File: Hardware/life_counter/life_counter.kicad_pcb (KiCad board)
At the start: 2 copper layers, 133.4 x 75.6 mm, 46 parts, among them J1 XIAO_BAT_LINK, P1 OLED-DISPLAY, Q1 Q-PMOS, U1 XIAO ESP32C3

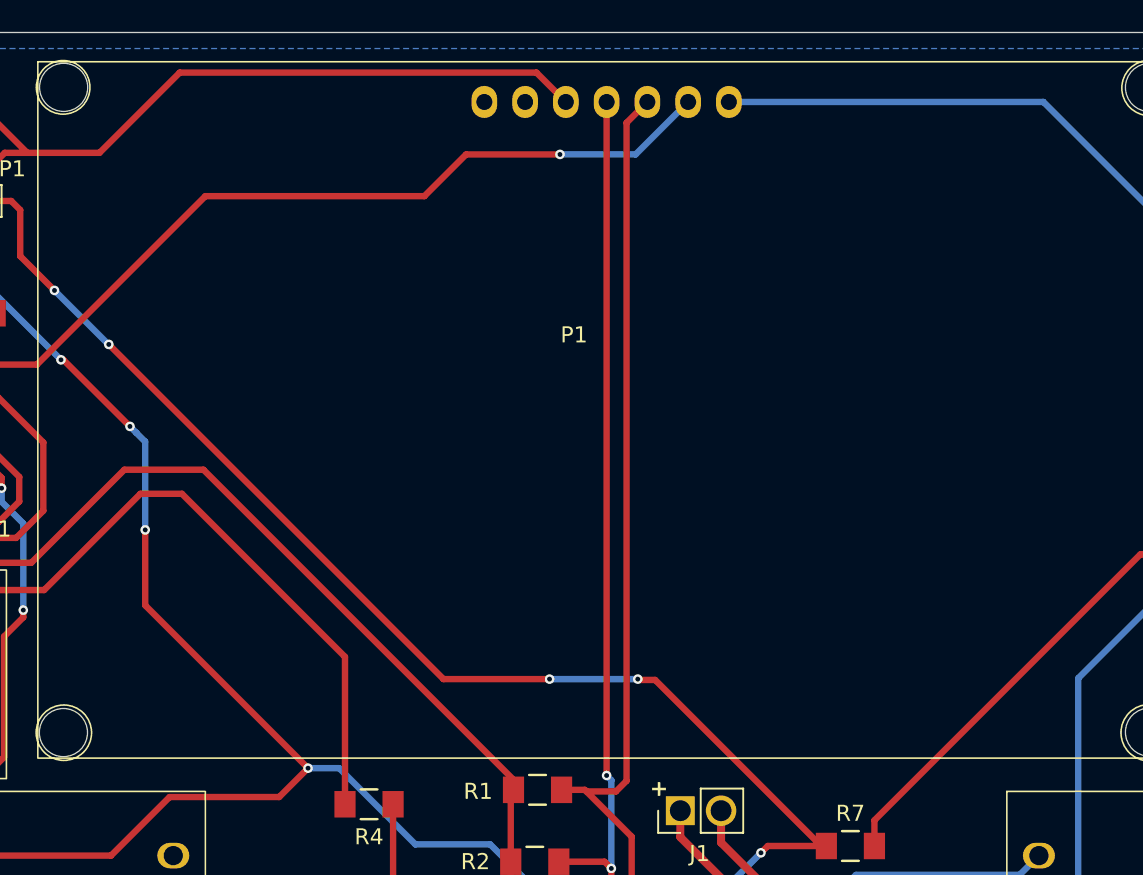
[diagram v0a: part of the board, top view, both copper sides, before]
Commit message: updated the kicad schematics, added auto shut off when battery is at 3.3V, added an image folder forthe  github page
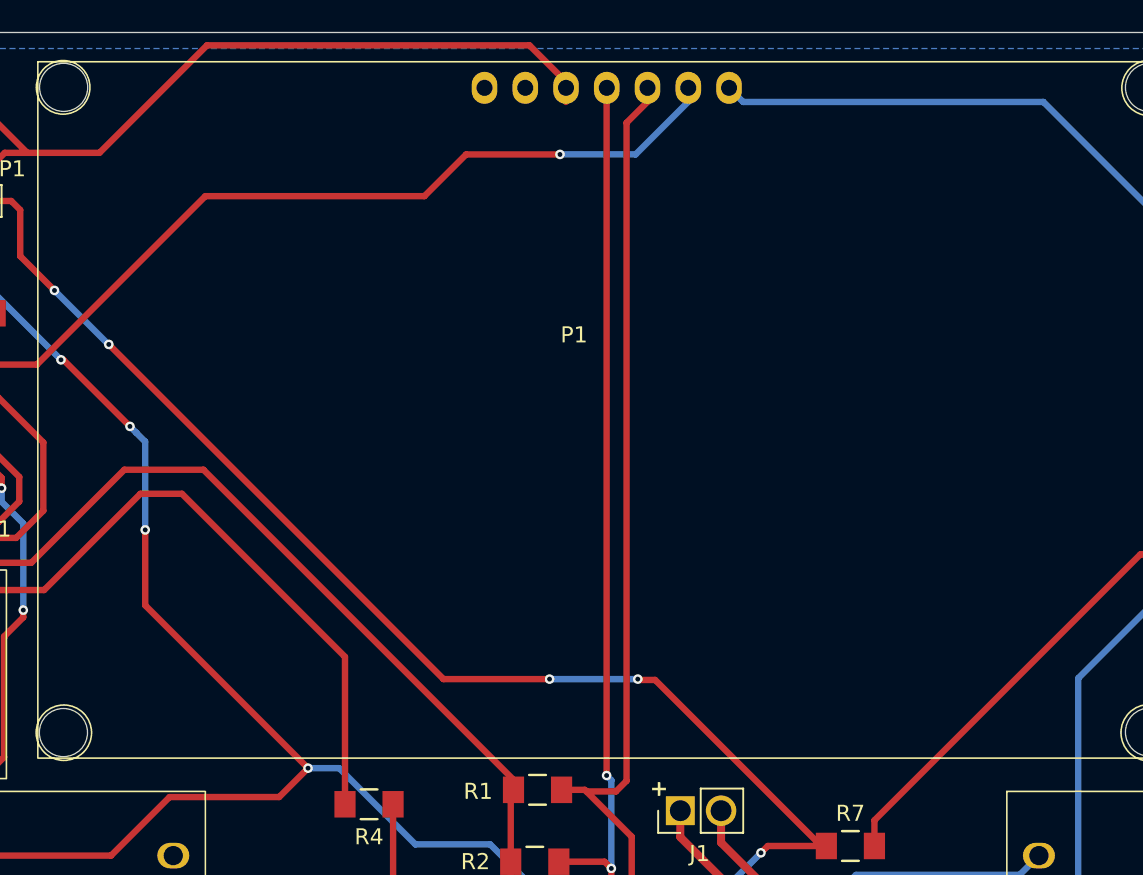
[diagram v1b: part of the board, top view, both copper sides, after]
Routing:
- net Net-(P1-RES): track 75.9 -> 78.0 mm
- net /SDA: track 64.3 -> 65.1 mm
- net /SCL: track 63.0 -> 63.9 mm
- net Net-(DISP_BYP1-B): track 87.8 -> 88.7 mm
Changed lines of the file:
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@@
 		)
 		(pad "1" thru_hole oval
-			(at 9.65 -15.02 270)
+			(at 9.66 -15.9 270)
 			(size 2 1.6)
 			(drill 1)
@@
 		)
 		(pad "2" thru_hole oval
-			(at 7.11 -15.02 90)
+			(at 7.12 -15.9 90)
 			(size 2 1.6)
 			(drill 1)
@@
 		)
 		(pad "3" thru_hole oval
-			(at 4.57 -15.02 90)
+			(at 4.58 -15.9 90)
 			(size 2 1.6)
 			(drill 1)
@@
 		)
 		(pad "4" thru_hole oval
-			(at 2.03 -15.02 90)
+			(at 2.04 -15.9 90)
 			(size 2 1.6)
 			(drill 1)
@@
 		)
 		(pad "5" thru_hole oval
-			(at -0.51 -15.02 90)
+			(at -0.5 -15.9 90)
 			(size 2 1.6)
 			(drill 1)
@@
 		)
 		(pad "6" thru_hole oval
-			(at -3.05 -15.02 90)
+			(at -3.04 -15.9 90)
 			(size 2 1.6)
 			(drill 1)
@@
 		)
 		(pad "7" thru_hole oval
-			(at -5.59 -15.02 90)
+			(at -5.58 -15.9 90)
 			(size 2 1.6)
 			(drill 1)
@@
 		)
 		(group ""
-			(members "c17f0be5-490c-4029-8d47-755324679b7e")
+			(members "2cb9cc7a-f7c2-4668-bdcf-35818d064778")
 		)
 		(group ""
-			(members "235958c5-d064-4237-962a-ab2f08b3ec1e")
+			(members "fbafe812-aa08-4744-bb48-69356cf10db5")
 		)
 		(embedded_fonts no)
@@
 	)
 	(gr_text "+"
-		(at 115.5 82.5 0)
+		(at 102.3 72.7 0)
 		(layer "F.SilkS")
 		(effects
@@
 	)
 	(gr_text "+"
-		(at 102.3 72.7 0)
+		(at 115.5 82.5 0)
 		(layer "F.SilkS")
 		(effects
@@
 	)
 	(segment
-		(start 134.55 37.05)
-		(end 143.6 37.05)
+		(start 126.8295 29.3295)
+		(end 134.55 37.05)
 		(width 0.4)
 		(layer "B.Cu")
@@
 	)
 	(segment
-		(start 107.2264 29.3295)
+		(start 108.1164 29.3295)
 		(end 126.8295 29.3295)
 		(width 0.4)
@@
 	)
 	(segment
-		(start 129 65.25)
-		(end 138.25 56)
+		(start 143.6 37.05)
+		(end 148.35 41.8)
 		(width 0.4)
 		(layer "B.Cu")
@@
 	)
 	(segment
-		(start 143.6 37.05)
-		(end 148.35 41.8)
+		(start 107.2364 28.4495)
+		(end 108.1164 29.3295)
+		(width 0.4)
+		(layer "B.Cu")
+		(net 3)
+	)
+	(segment
+		(start 129 65.25)
+		(end 138.25 56)
 		(width 0.4)
 		(layer "B.Cu")
@@
 	)
 	(segment
-		(start 126.8295 29.3295)
-		(end 134.55 37.05)
+		(start 110.211778 86.288222)
+		(end 117 79.5)
 		(width 0.4)
 		(layer "B.Cu")
@@
 	)
 	(segment
-		(start 110.211778 86.288222)
-		(end 117 79.5)
+		(start 134.55 37.05)
+		(end 143.6 37.05)
 		(width 0.4)
 		(layer "B.Cu")
@@
 	)
 	(segment
-		(start 99.6064 71.3064)
-		(end 99.6064 29.3295)
-		(width 0.4)
-		(layer "F.Cu")
-		(net 16)
-	)
-	(segment
 		(start 106.24 87.39)
 		(end 99.9 81.05)
@@
 	)
 	(segment
+		(start 99.6064 28.4595)
+		(end 99.6164 28.4495)
+		(width 0.4)
+		(layer "F.Cu")
+		(net 16)
+	)
+	(segment
 		(start 99.48 76.68)
 		(end 99.9 77.1)
@@
 		(net 16)
 	)
+	(segment
+		(start 99.6064 71.3064)
+		(end 99.6064 28.4595)
+		(width 0.4)
+		(layer "F.Cu")
+		(net 16)
+	)
 	(via
 		(at 99.6064 71.3064)
@@
 	)
 	(segment
-		(start 101.17 79.72475)
-		(end 101.17 75.12)
+		(start 102.1564 29.3195)
+		(end 100.849 30.6269)
 		(width 0.4)
 		(layer "F.Cu")
@@
 	)
 	(segment
-		(start 98.351 72.301)
-		(end 98.25 72.2)
+		(start 101.17 79.72475)
+		(end 101.17 75.12)
 		(width 0.4)
 		(layer "F.Cu")
@@
 	)
 	(segment
-		(start 102.1464 29.3295)
-		(end 100.849 30.6269)
+		(start 98.351 72.301)
+		(end 98.25 72.2)
 		(width 0.4)
 		(layer "F.Cu")
@@
 	)
 	(segment
+		(start 100.849 71.642364)
+		(end 100.190364 72.301)
+		(width 0.4)
+		(layer "F.Cu")
+		(net 17)
+	)
+	(segment
 		(start 100.849 30.6269)
 		(end 100.849 71.642364)
@@
 	)
 	(segment
-		(start 100.849 71.642364)
-		(end 100.190364 72.301)
+		(start 102.1564 28.4495)
+		(end 102.1564 29.3195)
 		(width 0.4)
 		(layer "F.Cu")
@@
 	)
 	(segment
-		(start 101.4159 32.6)
-		(end 96.7 32.6)
+		(start 104.6964 29.3195)
+		(end 101.4159 32.6)
 		(width 0.4)
 		(layer "B.Cu")
@@
 	)
 	(segment
-		(start 104.6864 29.3295)
-		(end 101.4159 32.6)
+		(start 104.6964 28.4495)
+		(end 104.6964 29.3195)
+		(width 0.4)
+		(layer "B.Cu")
+		(net 38)
+	)
+	(segment
+		(start 101.4159 32.6)
+		(end 96.7 32.6)
 		(width 0.4)
 		(layer "B.Cu")
@@
 	)
 	(segment
-		(start 59.85 34.748)
-		(end 62.098 32.5)
-		(width 0.4)
-		(layer "F.Cu")
-		(net 50)
-	)
-	(segment
-		(start 59.85 31.3741)
-		(end 59.85 35.5)
+		(start 97.0664 29.3295)
+		(end 97.0664 28.0664)
 		(width 0.4)
 		(layer "F.Cu")
@@
 	)
 	(segment
-		(start 73 27.5)
-		(end 68 32.5)
+		(start 59.85 34.748)
+		(end 62.098 32.5)
 		(width 0.4)
 		(layer "F.Cu")
@@
 	)
 	(segment
-		(start 97.0664 29.3295)
-		(end 95.2369 27.5)
+		(start 59.85 31.3741)
+		(end 59.85 35.5)
 		(width 0.4)
 		(layer "F.Cu")
@@
 	)
 	(segment
-		(start 95.2369 27.5)
-		(end 73 27.5)
+		(start 60.4986 29.5)
+		(end 60.4986 30.7255)
 		(width 0.4)
 		(layer "F.Cu")
@@
 	)
 	(segment
-		(start 60.4986 29.5)
-		(end 60.4986 30.7255)
+		(start 74.7 25.8)
+		(end 68 32.5)
 		(width 0.4)
 		(layer "F.Cu")
@@
 	)
 	(segment
-		(start 68 32.5)
-		(end 63.4986 32.5)
-		(width 0.4)
-		(layer "F.Cu")
-		(net 50)
-	)
-	(segment
 		(start 63.4986 32.5)
 		(end 60.4986 29.5)
@@
 	)
 	(segment
+		(start 97.0664 28.0664)
+		(end 94.8 25.8)
+		(width 0.4)
+		(layer "F.Cu")
+		(net 50)
+	)
+	(segment
+		(start 94.8 25.8)
+		(end 74.7 25.8)
+		(width 0.4)
+		(layer "F.Cu")
+		(net 50)
+	)
+	(segment
 		(start 50.4 26.5)
 		(end 59.6 26.5)
 		(width 0.4)
 		(layer "F.Cu")
+		(net 50)
+	)
+	(segment
+		(start 68 32.5)
+		(end 63.4986 32.5)
+		(width 0.4)
+		(layer "F.Cu")
